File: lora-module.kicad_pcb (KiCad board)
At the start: 4 copper layers, 27.3 x 24.5 mm, 8 parts, among them P1 CONN_01X07, P2 CONN_01X07, Q1 32MHz, U2 SX1276

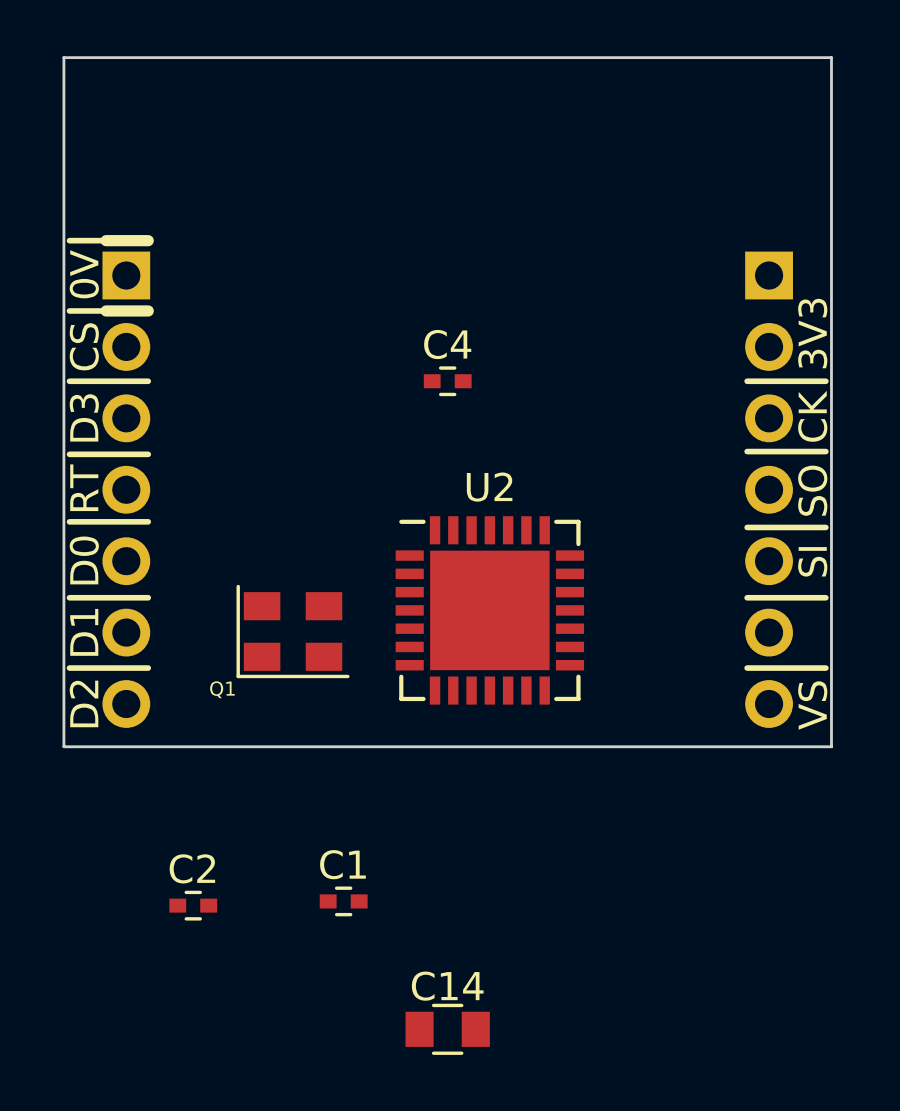
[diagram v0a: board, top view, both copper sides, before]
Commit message: added most of components to PCB
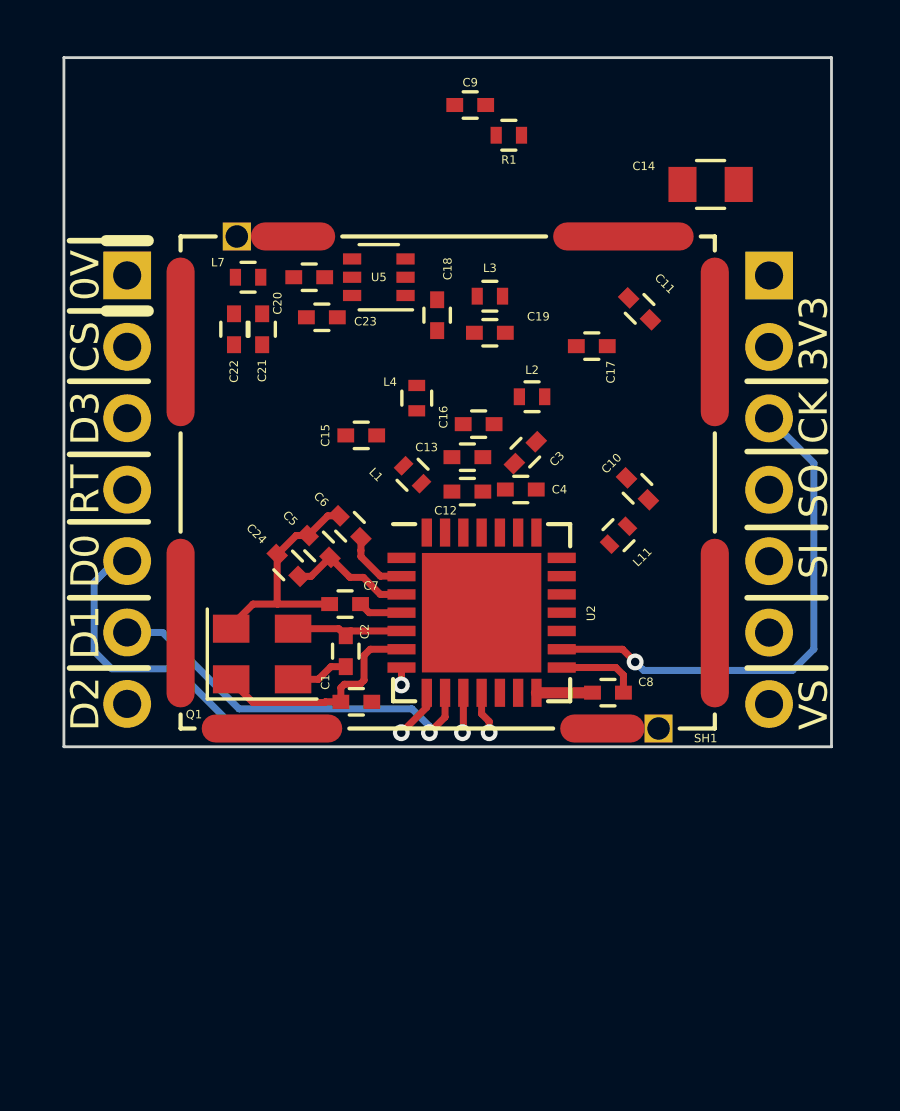
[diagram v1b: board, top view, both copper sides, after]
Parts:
- added C10: 3.3pF, Capacitors_SMD:C_0402, F.Cu at (105.4, 105.8)
- added C11: 47pF, Capacitors_SMD:C_0402, F.Cu at (105.5, 99.4)
- added C12: 10nF, Capacitors_SMD:C_0402, F.Cu at (99.3, 105.9)
- added C13: 47pF, Capacitors_SMD:C_0402, F.Cu at (99.3, 104.7)
- added C15: 8.2pF, Capacitors_SMD:C_0402, F.Cu at (95.6, 103.9)
- added C16: 22pF, Capacitors_SMD:C_0402, F.Cu at (99.8, 103.5)
- added C17: 8.2pF, Capacitors_SMD:C_0402, F.Cu at (103.8, 100.8)
- added C18: 1.5pF, Capacitors_SMD:C_0402, F.Cu at (98.3, 99.7)
- added C19: 3.3pF, Capacitors_SMD:C_0402, F.Cu at (100.2, 100.3)
- added C20: 47pF, Capacitors_SMD:C_0402, F.Cu at (93.7, 98.3)
- added C21: DNP, Capacitors_SMD:C_0402, F.Cu at (92.0, 100.2)
- added C22: DNP, Capacitors_SMD:C_0402, F.Cu at (91.0, 100.2)
- added C23: 1nF, Capacitors_SMD:C_0402, F.Cu at (94.2, 99.7)
- added C24: 47pF, Capacitors_SMD:C_0402, F.Cu at (93.0, 108.5)
- added C3: 47pF, Capacitors_SMD:C_0402, F.Cu at (101.4, 104.5)
- added C5: 100nF, Capacitors_SMD:C_0402, F.Cu at (94.1, 107.9)
- added C6: 100nF, Capacitors_SMD:C_0402, F.Cu at (95.2, 107.2)
- added C7: 100nF, Capacitors_SMD:C_0402, F.Cu at (95.0, 109.9)
- added C8: 100nF, Capacitors_SMD:C_0402, F.Cu at (104.3, 113.1)
- added C9: 1nF, Capacitors_SMD:C_0402, F.Cu at (99.5, 92.2)
- added L1: 2.2nH Wire, Inductors_SMD:L_0402, F.Cu at (97.4, 105.3)
- added L11: 10nH Wire, Inductors_SMD:L_0402, F.Cu at (104.7, 107.5)
- added L2: 5.6nH Wire, Inductors_SMD:L_0402, F.Cu at (101.7, 102.5)
- added L3: 4.7nH Wire, Inductors_SMD:L_0402, F.Cu at (100.2, 99.0)
- added L4: 33nH Wire, Inductors_SMD:L_0402, F.Cu at (97.5, 102.6)
- added L7: 0R, Inductors_SMD:L_0402, F.Cu at (91.5, 98.3)
- added R1: 1k, Resistors_SMD:R_0402, F.Cu at (100.8, 93.2)
- added SH1: RF_Shield_One_Piece, balcerzak-pcb:inAIR9B_shield, F.Cu at (98.7, 105.6)
- added U5: PE4259, TO_SOT_Packages_SMD:SOT-363_SC-70-6, F.Cu at (96.2, 98.3)
- moved C14 31.5 mm to (108.0, 95.0), turned to 180 degrees
- moved C2 10.6 mm to (95.0, 111.6), turned to 270 degrees
- moved C1 7.11 mm to (95.4, 113.4)
- moved C4 4.65 mm to (101.2, 105.8)
- moved Q1 1.36 mm to (92.0, 111.7)
- moved U2 0.30 mm to (99.9, 110.2)
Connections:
- P1 pad 2: Net-(P1-Pad2) -> /CS
- P1 pad 3: Net-(P1-Pad3) -> /DIO3
- P1 pad 4: Net-(P1-Pad4) -> /RST
- P1 pad 5: Net-(P1-Pad5) -> /DIO0
- P1 pad 6: Net-(P1-Pad6) -> /DIO1
- P1 pad 7: Net-(P1-Pad7) -> /DIO2
- P2 pad 3: Net-(P2-Pad3) -> /CLK
- P2 pad 4: Net-(P2-Pad4) -> /MISO
- P2 pad 5: Net-(P2-Pad5) -> /MOSI
- P2 pad 7: Net-(P2-Pad7) -> +3V3
- U2 pad 29: (no net) -> GND
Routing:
- net /DIO3: track 0.00 -> 23.8 mm, vias 0 -> 1
- net /CLK: track 0.00 -> 18.5 mm, vias 0 -> 1
- net /RST: track 0.00 -> 15.9 mm, vias 0 -> 1
- net /DIO2: track 0.00 -> 14.1 mm, vias 0 -> 1
- net /DIO1: track 0.00 -> 14.0 mm, vias 0 -> 1
- net GND: track 0.00 -> 13.5 mm
- net /DIO0: track 0.00 -> 12.3 mm, vias 0 -> 1
- net Net-(C1-Pad1): track 0.00 -> 8.02 mm
- net +3V3: track 0.00 -> 6.46 mm
- net Net-(C2-Pad1): track 0.00 -> 4.03 mm
- net Net-(C6-Pad1): track 0.00 -> 2.40 mm
- net Net-(C7-Pad1): track 0.00 -> 1.58 mm

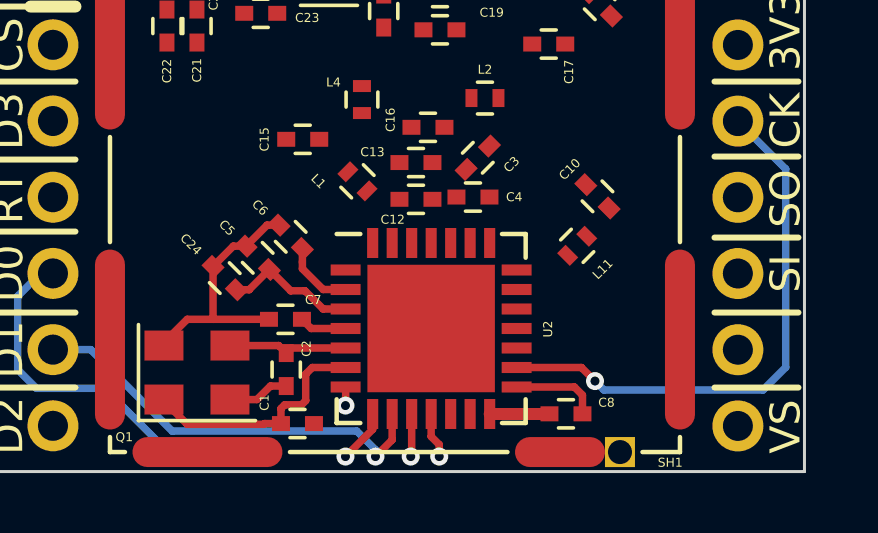
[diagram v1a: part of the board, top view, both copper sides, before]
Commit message: added all components description
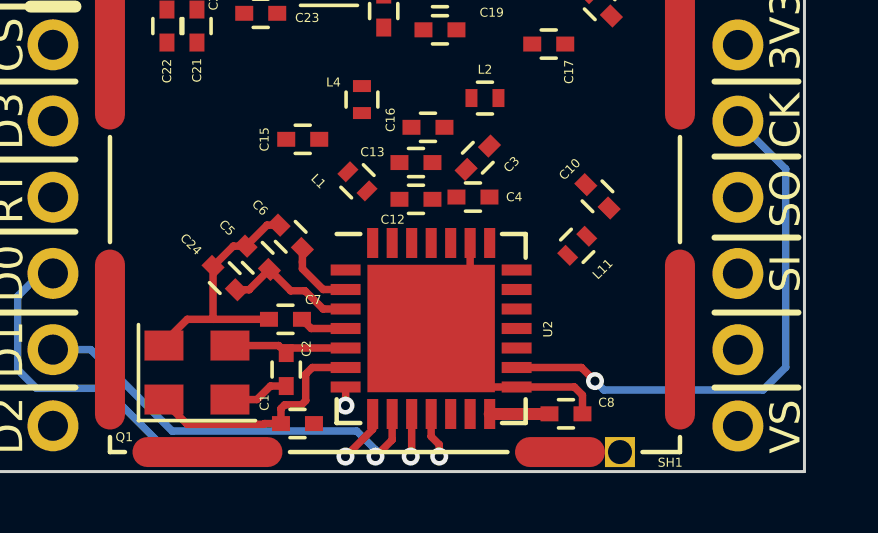
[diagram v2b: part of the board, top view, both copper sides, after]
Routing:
- net GND: track 13.5 -> 40.7 mm
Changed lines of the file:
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@@
   (general
     (links 102)
-    (no_connects 81)
-    (area 84.949999 90.439999 112.350001 115.050001)
+    (no_connects 83)
+    (area 84.949999 90.439999 112.57 115.42)
     (thickness 1.6)
     (drawings 30)
-    (tracks 103)
+    (tracks 122)
     (zones 0)
     (modules 37)
@@
   )
   (setup
-    (last_trace_width 0.5)
+    (last_trace_width 0.25)
     (user_trace_width 0.4)
     (user_trace_width 0.5)
@@
   (segment (start 101.80625 113.08125) (end 103.79375 113.08125) (width 0.4) (layer F.Cu) (net 1))
   (segment (start 103.79375 113.08125) (end 103.8 113.075) (width 0.4) (layer F.Cu) (net 1))
+  (segment (start 102.70625 112.18125) (end 101.80625 112.18125) (width 0.25) (layer F.Cu) (net 2))
+  (segment (start 101.80625 112.18125) (end 101.45 111.825) (width 0.25) (layer F.Cu) (net 2))
+  (segment (start 99.325 111.825) (end 98.2625 111.825) (width 0.25) (layer F.Cu) (net 2))
+  (segment (start 100.3875 111.825) (end 98.2625 111.825) (width 0.25) (layer F.Cu) (net 2))
+  (segment (start 100.3875 109.7) (end 99.325 109.7) (width 0.25) (layer F.Cu) (net 2))
+  (segment (start 100.3875 109.7) (end 101.45 109.7) (width 0.25) (layer F.Cu) (net 2))
+  (segment (start 99.325 110.7625) (end 98.2625 110.7625) (width 0.25) (layer F.Cu) (net 2))
+  (segment (start 98.2625 110.7625) (end 100.3875 110.7625) (width 0.25) (layer F.Cu) (net 2))
+  (segment (start 98.2625 111.825) (end 98.2625 110.7625) (width 0.25) (layer F.Cu) (net 2))
+  (segment (start 101.45 111.825) (end 98.2625 111.825) (width 0.25) (layer F.Cu) (net 2))
+  (segment (start 101.45 110.7625) (end 101.45 111.825) (width 0.25) (layer F.Cu) (net 2))
+  (segment (start 98.2625 110.7625) (end 101.45 110.7625) (width 0.25) (layer F.Cu) (net 2))
+  (segment (start 99.325 109.7) (end 99.325 110.7625) (width 0.25) (layer F.Cu) (net 2))
+  (segment (start 98.2625 109.7) (end 99.325 109.7) (width 0.25) (layer F.Cu) (net 2))
+  (segment (start 99.325 108.6375) (end 99.325 109.7) (width 0.25) (layer F.Cu) (net 2))
+  (segment (start 100.3875 108.6375) (end 99.325 108.6375) (width 0.25) (layer F.Cu) (net 2))
+  (segment (start 98.2625 108.6375) (end 101.45 108.6375) (width 0.25) (layer F.Cu) (net 2))
+  (segment (start 101.15625 107.38125) (end 101.15625 108.34375) (width 0.25) (layer F.Cu) (net 2))
+  (segment (start 101.15625 108.34375) (end 101.45 108.6375) (width 0.25) (layer F.Cu) (net 2))
   (segment (start 94.5 112.15) (end 95.025 112.15) (width 0.25) (layer F.Cu) (net 2))
   (segment (start 104.63125 112.18125) (end 104.9 112.45) (width 0.25) (layer F.Cu) (net 2))

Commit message: added PCB stack values
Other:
- board text added: "0.0355 mm"
- board text added: "0.0686 mm"
- board text added: "1 oz"
- board text added: "1.3 mm"
- board text added: "1.3000 mm"
- board text added: "1.4 mil"
- board text added: "1.5792 mm"
- board text added: "1080pp"
- board text added: "2.7 mil"
- board text added: "48.4 mil"
- board text added: "CORE"
- board text added: "KIKI PCB 4 layer stack"
- board text added: "L1 Signal"
- board text added: "L2 GND"
- board text added: "L3 Power"
- board text added: "L4 Signal"
- board text added: "pre-preg"
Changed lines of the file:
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@@
   (general
     (links 102)
-    (no_connects 83)
+    (no_connects 67)
     (area 84.949999 90.439999 112.57 115.42)
     (thickness 1.6)
-    (drawings 30)
+    (drawings 65)
     (tracks 122)
     (zones 0)
@@
     )
   )
+  (gr_text "KIKI PCB 4 layer stack " (at 149 89) (layer Dwgs.User)
+    (effects (font (size 1.5 1.5) (thickness 0.3)))
+  )
+  (gr_text "1.5792 mm" (at 170 117) (layer Dwgs.User)
+    (effects (font (size 1.5 1.5) (thickness 0.3)) (justify left))
+  )
+  (gr_line (start 135 115) (end 184 115) (layer Dwgs.User) (width 0.2))
+  (gr_text "1.3000 mm" (at 170 104) (layer Dwgs.User)
+    (effects (font (size 1.5 1.5) (thickness 0.3)) (justify left))
+  )
+  (gr_text "0.0686 mm" (at 170 110) (layer Dwgs.User)
+    (effects (font (size 1.5 1.5) (thickness 0.3)) (justify left))
+  )
+  (gr_text "0.0355 mm" (at 170 101) (layer Dwgs.User)
+    (effects (font (size 1.5 1.5) (thickness 0.3)) (justify left))
+  )
+  (gr_text "0.0355 mm" (at 170 107) (layer Dwgs.User)
+    (effects (font (size 1.5 1.5) (thickness 0.3)) (justify left))
+  )
+  (gr_text "0.0355 mm" (at 170 113) (layer Dwgs.User)
+    (effects (font (size 1.5 1.5) (thickness 0.3)) (justify left))
+  )
+  (gr_text "0.0686 mm" (at 170 98) (layer Dwgs.User)
+    (effects (font (size 1.5 1.5) (thickness 0.3)) (justify left))
+  )
+  (gr_text "0.0355 mm" (at 170 95) (layer Dwgs.User)
+    (effects (font (size 1.5 1.5) (thickness 0.3)) (justify left))
+  )
+  (gr_text "1.4 mil" (at 158 113) (layer Dwgs.User)
+    (effects (font (size 1.5 1.5) (thickness 0.3)) (justify left))
+  )
+  (gr_text "2.7 mil" (at 158 110) (layer Dwgs.User)
+    (effects (font (size 1.5 1.5) (thickness 0.3)) (justify left))
+  )
+  (gr_text 1080pp (at 147 110) (layer Dwgs.User)
+    (effects (font (size 1.5 1.5) (thickness 0.3)) (justify left))
+  )
+  (gr_text "1.4 mil" (at 158 107) (layer Dwgs.User)
+    (effects (font (size 1.5 1.5) (thickness 0.3)) (justify left))
+  )
+  (gr_text "48.4 mil" (at 158 104) (layer Dwgs.User)
+    (effects (font (size 1.5 1.5) (thickness 0.3)) (justify left))
+  )
+  (gr_text "1.4 mil" (at 158 101) (layer Dwgs.User)
+    (effects (font (size 1.5 1.5) (thickness 0.3)) (justify left))
+  )
+  (gr_text "1 oz" (at 147 101) (layer Dwgs.User)
+    (effects (font (size 1.5 1.5) (thickness 0.3)) (justify left))
+  )
+  (gr_text "1 oz" (at 147 113) (layer Dwgs.User)
+    (effects (font (size 1.5 1.5) (thickness 0.3)) (justify left))
+  )
+  (gr_text "1 oz" (at 147 107) (layer Dwgs.User)
+    (effects (font (size 1.5 1.5) (thickness 0.3)) (justify left))
+  )
+  (gr_text 1080pp (at 147 98) (layer Dwgs.User)
+    (effects (font (size 1.5 1.5) (thickness 0.3)) (justify left))
+  )
+  (gr_text "1.3 mm" (at 147 104) (layer Dwgs.User)
+    (effects (font (size 1.5 1.5) (thickness 0.3)) (justify left))
+  )
+  (gr_text pre-preg (at 135 110) (layer Dwgs.User)
+    (effects (font (size 1.5 1.5) (thickness 0.3)) (justify left))
+  )
+  (gr_text pre-preg (at 135 98) (layer Dwgs.User)
+    (effects (font (size 1.5 1.5) (thickness 0.3)) (justify left))
+  )
+  (gr_text CORE (at 135 104) (layer Dwgs.User)
+    (effects (font (size 1.5 1.5) (thickness 0.3)) (justify left))
+  )
+  (gr_text "L4 Signal" (at 135 113) (layer Dwgs.User)
+    (effects (font (size 1.5 1.5) (thickness 0.3)) (justify left))
+  )
+  (gr_text "L3 Power" (at 135 107) (layer Dwgs.User)
+    (effects (font (size 1.5 1.5) (thickness 0.3)) (justify left))
+  )
+  (gr_text "L2 GND" (at 135 101) (layer Dwgs.User)
+    (effects (font (size 1.5 1.5) (thickness 0.3)) (justify left))
+  )
+  (gr_text "2.7 mil" (at 158 98) (layer Dwgs.User)
+    (effects (font (size 1.5 1.5) (thickness 0.3)) (justify left))
+  )
+  (gr_text "1.4 mil" (at 158 95) (layer Dwgs.User)
+    (effects (font (size 1.5 1.5) (thickness 0.3)) (justify left))
+  )
+  (gr_text "1 oz" (at 147 95) (layer Dwgs.User)
+    (effects (font (size 1.5 1.5) (thickness 0.3)) (justify left))
+  )
+  (gr_text "L1 Signal" (at 135 95) (layer Dwgs.User)
+    (effects (font (size 1.5 1.5) (thickness 0.3)) (justify left))
+  )
+  (gr_line (start 169 91) (end 169 117) (layer Dwgs.User) (width 0.2))
+  (gr_line (start 157 91) (end 157 117) (layer Dwgs.User) (width 0.2))
+  (gr_line (start 146 91) (end 146 117) (layer Dwgs.User) (width 0.2))
+  (gr_line (start 135 93) (end 184 93) (layer Dwgs.User) (width 0.2))
   (gr_line (start 86.5 99.5) (end 88 99.5) (layer F.SilkS) (width 0.4))
   (gr_line (start 86.5 97) (end 88 97) (layer F.SilkS) (width 0.4))
